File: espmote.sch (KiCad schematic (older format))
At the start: 33 parts, among them J1 Serial, J2 Line, U1 ESP-12E, U2 LM1117-3.3, U3 H11AA1, U4 MOC3023M, U5 H11AA1, U6 MOC3023M, U7 H11AA1, U8 MOC3023M, U9 HLK-PM01

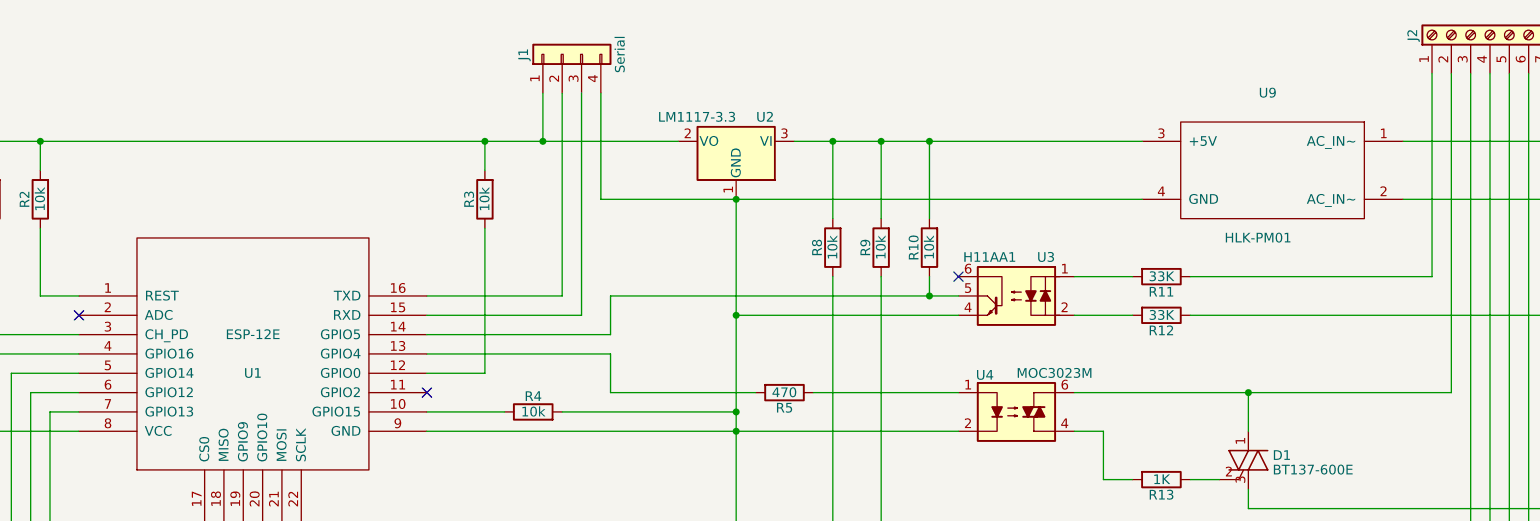
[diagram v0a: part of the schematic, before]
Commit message: Use ESP-12E component from pniaps library
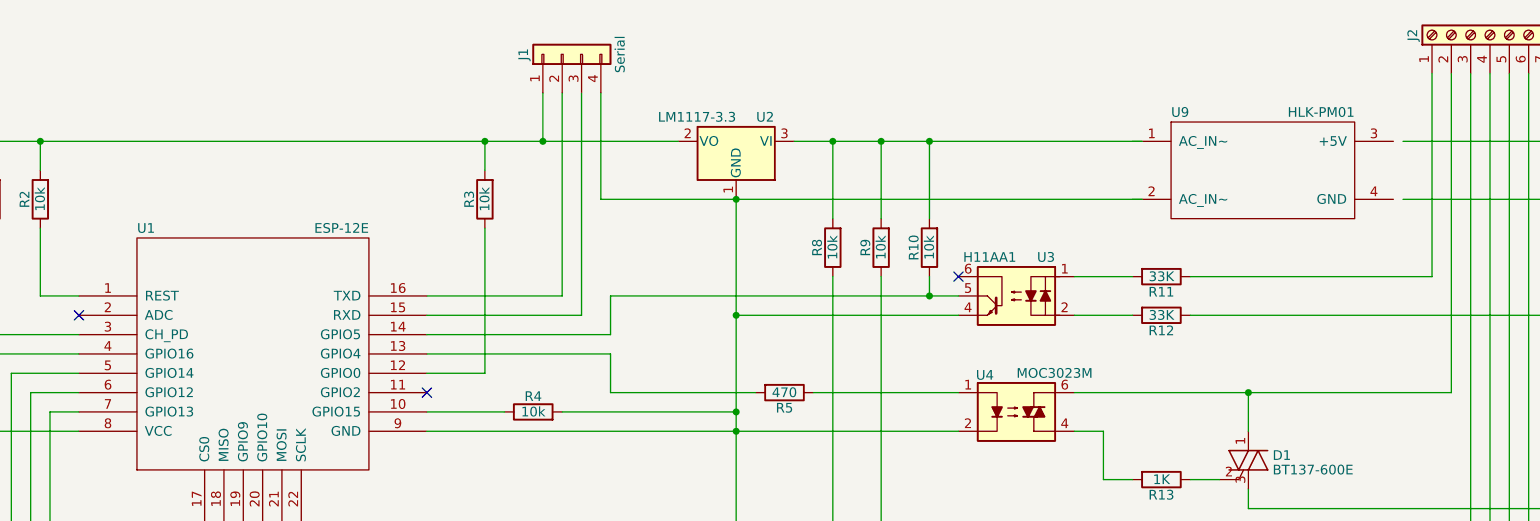
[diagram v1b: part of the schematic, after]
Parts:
- U1: footprint ESP8266:ESP-12E -> pniaps:ESP-12E
- U9: footprint pniaps_lib:HLK-PM01 -> pniaps:HLK-PM01
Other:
- moved on the sheet: U9
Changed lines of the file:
@@
 LIBS:contrib
 LIBS:valves
-LIBS:pnia_kicad
+LIBS:pniaps_kicad
 LIBS:ESP8266
 LIBS:espmote-cache
-EELAYER 25 0
+EELAYER 26 0
 EELAYER END
 $Descr A4 11693 8268
@@
 U 1 1 59A361F9
 P 9000 1500
-F 0 "U9" H 9000 1900 50  0000 C CNN
-F 1 "HLK-PM01" H 9050 1150 50  0000 C CNN
-F 2 "pniaps_lib:HLK-PM01" H 9000 1500 50  0001 C CNN
+F 0 "U9" H 8500 1800 50  0000 L CNN
+F 1 "HLK-PM01" H 9450 1800 50  0000 R CNN
+F 2 "pniaps:HLK-PM01" H 9000 1200 50  0001 C CNN
 F 3 "" H 9000 1500 50  0000 C CNN
 	1    9000 1500
-	-1   0    0    -1
+	1    0    0    -1
 $EndComp
 $Comp
@@
 U 1 1 59A36270
 P 3750 2450
-F 0 "U1" H 3750 2350 50  0000 C CNN
-F 1 "ESP-12E" H 3750 2550 50  0000 C CNN
-F 2 "ESP8266:ESP-12E" H 3750 2450 50  0001 C CNN
+F 0 "U1" H 3150 3100 50  0000 L CNN
+F 1 "ESP-12E" H 4350 3100 50  0000 R CNN
+F 2 "pniaps:ESP-12E" H 3750 2950 50  0001 C CNN
 F 3 "" H 3750 2450 50  0001 C CNN
 	1    3750 2450
@@
 F 0 "U7" H 7500 5250 50  0000 L CNN
 F 1 "H11AA1" H 7700 5250 50  0000 L CNN
-F 2 "Housings_DIP:DIP-6_W7.62mm" H 7500 4850 50  0001 L CIN
+F 2 "Housings_DIP:DIP-6_W7.62mm" H 7700 4850 50  0001 C CIN
 F 3 "" H 7700 5050 50  0001 L CNN
 	1    7700 5050
@@
 F 0 "U5" H 7500 3850 50  0000 L CNN
 F 1 "H11AA1" H 7700 3850 50  0000 L CNN
-F 2 "Housings_DIP:DIP-6_W7.62mm" H 7500 3450 50  0001 L CIN
+F 2 "Housings_DIP:DIP-6_W7.62mm" H 7700 3450 50  0001 C CIN
 F 3 "" H 7700 3650 50  0001 L CNN
 	1    7700 3650
@@
 F 0 "U3" H 7500 2350 50  0000 L CNN
 F 1 "H11AA1" H 7700 2350 50  0000 L CNN
-F 2 "Housings_DIP:DIP-6_W7.62mm" H 7500 1950 50  0001 L CIN
+F 2 "Housings_DIP:DIP-6_W7.62mm" H 7700 1950 50  0001 C CIN
 F 3 "" H 7700 2150 50  0001 L CNN
 	1    7700 2150

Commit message: two channels and pcb
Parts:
- removed D1: BT137-600E, TO_SOT_Packages_THT:TO-220_Vertical, symbol Q_TRIAC_AGA
- removed R10: 10k, Resistors_SMD:R_1206_HandSoldering, symbol R
- removed R11, R12: 33K, Resistors_THT:R_Axial_DIN0414_L11.9mm_D4.5mm_P15.24mm_Horizontal, symbol R
- removed R13: 1K, Resistors_SMD:R_1206_HandSoldering, symbol R
- removed R5: 470, Resistors_SMD:R_1206_HandSoldering, symbol R
- removed U3: H11AA1, Housings_DIP:DIP-6_W7.62mm, symbol H11AA1
- removed U4: MOC3023M, Housings_DIP:DIP-6_W7.62mm, symbol MOC3023M
- J2: footprint Pin_Headers:Pin_Header_Straight_1x08_Pitch2.54mm -> Connectors_Terminal_Blocks:TerminalBlock_Pheonix_MKDS1.5-6pol; symbol Screw_Terminal_01x08 -> Screw_Terminal_01x06
- R14, R15, R17, R18: footprint Resistors_THT:R_Axial_DIN0414_L11.9mm_D4.5mm_P15.24mm_Horizontal -> Resistors_SMD:R_2512_HandSoldering
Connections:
- wire segments 102 -> 78
- no-connect marks 11 -> 12
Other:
- moved on the sheet: U2, U9
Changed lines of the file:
@@
 LIBS:contrib
 LIBS:valves
-LIBS:pniaps_kicad
+LIBS:pniaps
 LIBS:ESP8266
 LIBS:espmote-cache
@@
 F 3 "" H 9000 1500 50  0000 C CNN
 	1    9000 1500
-	1    0    0    -1
+	-1   0    0    -1
 $EndComp
 $Comp
@@
 L LM1117-3.3 U2
 U 1 1 59A3640F
-P 6250 1350
-F 0 "U2" H 6100 1475 50  0000 C CNN
-F 1 "LM1117-3.3" H 6250 1475 50  0000 L CNN
-F 2 "TO_SOT_Packages_THT:TO-220_Vertical" H 6250 1350 50  0001 C CNN
-F 3 "" H 6250 1350 50  0001 C CNN
-	1    6250 1350
+P 7500 1350
+F 0 "U2" H 7350 1475 50  0000 C CNN
+F 1 "LM1117-3.3" H 7500 1475 50  0000 L CNN
+F 2 "TO_SOT_Packages_THT:TO-220_Vertical" H 7500 1350 50  0001 C CNN
+F 3 "" H 7500 1350 50  0001 C CNN
+	1    7500 1350
 	-1   0    0    -1
 $EndComp
@@
 $EndComp
 $Comp
-L Screw_Terminal_01x08 J2
+L Screw_Terminal_01x06 J2
 U 1 1 59A37682
-P 10150 800
-F 0 "J2" H 10150 1200 50  0000 C CNN
-F 1 "Line" H 10150 300 50  0000 C CNN
-F 2 "Pin_Headers:Pin_Header_Straight_1x08_Pitch2.54mm" H 10150 800 50  0001 C CNN
-F 3 "" H 10150 800 50  0001 C CNN
-	1    10150 800
-	0    -1   -1   0
+P 10350 800
+F 0 "J2" H 10350 1200 50  0000 C CNN
+F 1 "Line" H 10350 300 50  0000 C CNN
+F 2 "Connectors_Terminal_Blocks:TerminalBlock_Pheonix_MKDS1.5-6pol" H 10350 800 50  0001 C CNN
+F 3 "" H 10350 800 50  0001 C CNN
+	1    10350 800
+	0    1    -1   0
 $EndComp
 $Comp
@@
 Wire Wire Line
 	8150 4600 8300 4600
-$Comp
-L MOC3023M U4
-U 1 1 59A51C8E
-P 7700 2750
-F 0 "U4" H 7490 2940 50  0000 L CNN
-F 1 "MOC3023M" H 7700 2950 50  0000 L CNN
-F 2 "Housings_DIP:DIP-6_W7.62mm" H 7500 2550 50  0001 L CIN
-F 3 "" H 7675 2750 50  0001 L CNN
-	1    7700 2750
-	1    0    0    -1
-$EndComp
-$Comp
-L H11AA1 U3
-U 1 1 59A51C94
-P 7700 2150
-F 0 "U3" H 7500 2350 50  0000 L CNN
-F 1 "H11AA1" H 7700 2350 50  0000 L CNN
-F 2 "Housings_DIP:DIP-6_W7.62mm" H 7700 1950 50  0001 C CIN
-F 3 "" H 7700 2150 50  0001 L CNN
-	1    7700 2150
-	-1   0    0    -1
-$EndComp
-$Comp
-L Q_TRIAC_AGA D1
-U 1 1 59A51C9A
-P 8900 3000
-F 0 "D1" H 9025 3025 50  0000 L CNN
-F 1 "BT137-600E" H 9025 2950 50  0000 L CNN
-F 2 "TO_SOT_Packages_THT:TO-220_Vertical" V 8975 3025 50  0001 C CNN
-F 3 "" V 8900 3000 50  0001 C CNN
-	1    8900 3000
-	1    0    0    -1
-$EndComp
-$Comp
-L R R13
-U 1 1 59A51CA0
-P 8450 3100
-F 0 "R13" V 8530 3100 50  0000 C CNN
-F 1 "1K" V 8450 3100 50  0000 C CNN
-F 2 "Resistors_SMD:R_1206_HandSoldering" V 8380 3100 50  0001 C CNN
-F 3 "" H 8450 3100 50  0001 C CNN
-	1    8450 3100
-	0    1    1    0
-$EndComp
-$Comp
-L R R5
-U 1 1 59A51CA7
-P 6500 2650
-F 0 "R5" V 6580 2650 50  0000 C CNN
-F 1 "470" V 6500 2650 50  0000 C CNN
-F 2 "Resistors_SMD:R_1206_HandSoldering" V 6430 2650 50  0001 C CNN
-F 3 "" H 6500 2650 50  0001 C CNN
-	1    6500 2650
-	0    1    1    0
-$EndComp
-Wire Wire Line
-	8000 2850 8150 2850
-Wire Wire Line
-	8150 2850 8150 3100
-Wire Wire Line
-	8150 3100 8300 3100
 Wire Wire Line
 	8000 5550 10350 5550
@@
 	10150 4150 10150 1000
 Wire Wire Line
-	8000 2650 9950 2650
-Wire Wire Line
-	9950 2650 9950 1000
-Wire Wire Line
-	8900 3150 8900 3250
-Wire Wire Line
 	8900 4650 8900 4750
-Wire Wire Line
-	8900 2850 8900 2650
-Connection ~ 8900 2650
 Wire Wire Line
 	8900 4350 8900 4150
@@
 	8900 5750 8900 5550
 Connection ~ 8900 5550
-$Comp
-L R R11
-U 1 1 59A52964
-P 8450 2050
-F 0 "R11" V 8530 2050 50  0000 C CNN
-F 1 "33K" V 8450 2050 50  0000 C CNN
-F 2 "Resistors_THT:R_Axial_DIN0414_L11.9mm_D4.5mm_P15.24mm_Horizontal" V 8380 2050 50  0001 C CNN
-F 3 "" H 8450 2050 50  0001 C CNN
-	1    8450 2050
-	0    1    1    0
-$EndComp
-$Comp
-L R R12
-U 1 1 59A52C17
-P 8450 2250
-F 0 "R12" V 8530 2250 50  0000 C CNN
-F 1 "33K" V 8450 2250 50  0000 C CNN
-F 2 "Resistors_THT:R_Axial_DIN0414_L11.9mm_D4.5mm_P15.24mm_Horizontal" V 8380 2250 50  0001 C CNN
-F 3 "" H 8450 2250 50  0001 C CNN
-	1    8450 2250
-	0    1    1    0
-$EndComp
 $Comp
 L R R14
@@
 F 0 "R14" V 8530 3550 50  0000 C CNN
 F 1 "33K" V 8450 3550 50  0000 C CNN
-F 2 "Resistors_THT:R_Axial_DIN0414_L11.9mm_D4.5mm_P15.24mm_Horizontal" V 8380 3550 50  0001 C CNN
+F 2 "Resistors_SMD:R_2512_HandSoldering" V 8380 3550 50  0001 C CNN
 F 3 "" H 8450 3550 50  0001 C CNN
 	1    8450 3550
@@
 F 0 "R15" V 8530 3750 50  0000 C CNN
 F 1 "33K" V 8450 3750 50  0000 C CNN
-F 2 "Resistors_THT:R_Axial_DIN0414_L11.9mm_D4.5mm_P15.24mm_Horizontal" V 8380 3750 50  0001 C CNN
+F 2 "Resistors_SMD:R_2512_HandSoldering" V 8380 3750 50  0001 C CNN
 F 3 "" H 8450 3750 50  0001 C CNN
 	1    8450 3750
@@
 F 0 "R17" V 8530 4950 50  0000 C CNN
 F 1 "33K" V 8450 4950 50  0000 C CNN
-F 2 "Resistors_THT:R_Axial_DIN0414_L11.9mm_D4.5mm_P15.24mm_Horizontal" V 8380 4950 50  0001 C CNN
+F 2 "Resistors_SMD:R_2512_HandSoldering" V 8380 4950 50  0001 C CNN
 F 3 "" H 8450 4950 50  0001 C CNN
 	1    8450 4950
@@
 F 0 "R18" V 8530 5150 50  0000 C CNN
 F 1 "33K" V 8450 5150 50  0000 C CNN
-F 2 "Resistors_THT:R_Axial_DIN0414_L11.9mm_D4.5mm_P15.24mm_Horizontal" V 8380 5150 50  0001 C CNN
+F 2 "Resistors_SMD:R_2512_HandSoldering" V 8380 5150 50  0001 C CNN
 F 3 "" H 8450 5150 50  0001 C CNN
 	1    8450 5150
@@
 $EndComp
 Wire Wire Line
-	8000 2050 8300 2050
-Wire Wire Line
-	8300 2250 8000 2250
-Wire Wire Line
 	8000 3550 8300 3550
 Wire Wire Line
@@
 	8300 5150 8000 5150
 Wire Wire Line
-	6250 2250 7400 2250
-Wire Wire Line
 	6250 5150 7400 5150
 Wire Wire Line
 	6250 3750 7400 3750
 Wire Wire Line
-	2150 1350 5950 1350
+	2150 1350 7200 1350
 Wire Wire Line
 	5250 1100 5250 1350
@@
 	5450 1100 5450 2250
 Wire Wire Line
-	6550 1350 8350 1350
-Wire Wire Line
 	5550 1650 8350 1650
 Wire Wire Line
 	6250 1650 6250 5750
 Connection ~ 6250 3750
-Connection ~ 6250 2250
 Wire Wire Line
 	5550 1100 5550 1650
 Connection ~ 6250 1650
 Wire Wire Line
-	8600 2050 9850 2050
-Wire Wire Line
-	9850 2050 9850 1000
-Wire Wire Line
 	8600 3550 10050 3550
 Wire Wire Line
@@
 Wire Wire Line
 	10550 1000 10550 5150
-Wire Wire Line
-	10550 2250 8600 2250
-Wire Wire Line
-	8900 3250 10450 3250
-Connection ~ 10450 3250
 Wire Wire Line
 	8900 4750 10450 4750
@@
 Wire Wire Line
 	10550 3750 8600 3750
-Connection ~ 10550 2250
 Wire Wire Line
 	10550 5150 8600 5150
@@
 Wire Wire Line
 	2400 2450 2400 5550
-$Comp
-L R R10
-U 1 1 59A61875
-P 7250 1900
-F 0 "R10" V 7330 1900 50  0000 C CNN
-F 1 "10k" V 7250 1900 50  0000 C CNN
-F 2 "Resistors_SMD:R_1206_HandSoldering" V 7180 1900 50  0001 C CNN
-F 3 "" H 7250 1900 50  0001 C CNN
-	1    7250 1900
-	-1   0    0    1
-$EndComp
 $Comp
 L R R9
@@
 $EndComp
 Wire Wire Line
-	7250 1750 7250 1350
-Connection ~ 7250 1350
-Wire Wire Line
-	7000 1750 7000 1350
+	7000 1350 7000 1750
 Connection ~ 7000 1350
 Wire Wire Line
-	6750 1750 6750 1350
+	6750 1350 6750 1750
 Connection ~ 6750 1350
-Wire Wire Line
-	7250 2050 7250 2150
-Connection ~ 7250 2150
 Wire Wire Line
 	7000 2050 7000 3650
@@
 	4650 2750 5050 2750
 Wire Wire Line
-	4650 2850 7400 2850
-Connection ~ 6250 2850
-Wire Wire Line
 	5350 2750 6250 2750
 Connection ~ 6250 2750
 Wire Wire Line
-	5600 2650 6350 2650
-Wire Wire Line
-	6650 2650 7400 2650
-Wire Wire Line
 	4950 2550 4650 2550
-Wire Wire Line
-	5600 2650 5600 2450
-Wire Wire Line
-	5600 2450 4650 2450
-Wire Wire Line
-	5600 2150 7400 2150
-Wire Wire Line
-	5600 2150 5600 2350
-Wire Wire Line
-	5600 2350 4650 2350
 Wire Wire Line
 	5350 2150 4650 2150
@@
 Wire Wire Line
 	2400 5550 6350 5550
-NoConn ~ 7400 2050
 NoConn ~ 7400 3550
 NoConn ~ 7400 4950
 Wire Wire Line
-	8600 3100 8750 3100
-Wire Wire Line
 	8600 4600 8750 4600
 Wire Wire Line
 	8600 6000 8750 6000
+Wire Wire Line
+	4650 2850 6250 2850
+Connection ~ 6250 2850
+NoConn ~ 4650 2450
+NoConn ~ 4650 2350
+Connection ~ 7500 1650
+Wire Wire Line
+	7800 1350 8350 1350
 $EndSCHEMATC

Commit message: Remove detectors
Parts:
- removed R14, R15, R17, R18: 33K, Resistors_SMD:R_2512_HandSoldering, symbol R
- removed R8, R9: 10k, Resistors_SMD:R_1206_HandSoldering, symbol R
- removed U5, U7: H11AA1, Housings_DIP:DIP-6_W7.62mm, symbol H11AA1
- added J3: Switch, Connectors_Terminal_Blocks:TerminalBlock_Pheonix_MKDS1.5-4pol, symbol Screw_Terminal_01x04
- J2: footprint Connectors_Terminal_Blocks:TerminalBlock_Pheonix_MKDS1.5-6pol -> Connectors_Terminal_Blocks:TerminalBlock_Pheonix_MKDS1.5-4pol; symbol Screw_Terminal_01x06 -> Screw_Terminal_01x04
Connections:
- net at J1.4 (Pin_4), R4.2, U1.9 (GND)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: now also J3.2 (Pin_2)
- net at U1.5 (GPIO14): now also J3.4 (Pin_4)
- net at U1.7 (GPIO13): now also J3.3 (Pin_3)
- net at J1.1 (Pin_1), R1.2, R2.2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: now also J3.1 (Pin_1)
- net at J2.4 (Pin_4): now also D2.1 (A1), U6.6
- no-connect marks 12 -> 10
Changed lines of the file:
@@
-$EndComp
-$Comp
-L ESP-12E U1
-U 1 1 59A36270
-P 3750 2450
-F 0 "U1" H 3150 3100 50  0000 L CNN
-F 1 "ESP-12E" H 4350 3100 50  0000 R CNN
-F 2 "pniaps:ESP-12E" H 3750 2950 50  0001 C CNN
-F 3 "" H 3750 2450 50  0001 C CNN
-	1    3750 2450
-	1    0    0    -1
 $EndComp
 $Comp
@@
 $EndComp
 $Comp
-L H11AA1 U7
-U 1 1 59A375C1
-P 7700 5050
-F 0 "U7" H 7500 5250 50  0000 L CNN
-F 1 "H11AA1" H 7700 5250 50  0000 L CNN
-F 2 "Housings_DIP:DIP-6_W7.62mm" H 7700 4850 50  0001 C CIN
-F 3 "" H 7700 5050 50  0001 L CNN
-	1    7700 5050
-	-1   0    0    -1
-$EndComp
-$Comp
-L Screw_Terminal_01x06 J2
+L Screw_Terminal_01x04 J2
 U 1 1 59A37682
-P 10350 800
-F 0 "J2" H 10350 1200 50  0000 C CNN
-F 1 "Line" H 10350 300 50  0000 C CNN
-F 2 "Connectors_Terminal_Blocks:TerminalBlock_Pheonix_MKDS1.5-6pol" H 10350 800 50  0001 C CNN
-F 3 "" H 10350 800 50  0001 C CNN
-	1    10350 800
+P 10450 800
+F 0 "J2" V 10500 1000 50  0000 L CNN
+F 1 "Line" V 10400 1000 50  0000 L CNN
+F 2 "Connectors_Terminal_Blocks:TerminalBlock_Pheonix_MKDS1.5-4pol" H 10450 800 50  0001 C CNN
+F 3 "" H 10450 800 50  0001 C CNN
+	1    10450 800
 	0    1    -1   0
 $EndComp
@@
 U 1 1 59A4F8A3
 P 5350 900
-F 0 "J1" H 5350 1100 50  0000 C CNN
-F 1 "Serial" H 5350 600 50  0000 C CNN
+F 0 "J1" V 5400 600 50  0000 R CNN
+F 1 "Serial" V 5300 600 50  0000 R CNN
 F 2 "Pin_Headers:Pin_Header_Straight_1x04_Pitch2.54mm" H 5350 900 50  0001 C CNN
 F 3 "" H 5350 900 50  0001 C CNN
@@
 NoConn ~ 4650 2650
 Wire Wire Line
-	2150 1350 2150 2850
+	2150 1000 2150 2850
 Wire Wire Line
 	8000 5750 8150 5750
@@
 	1    7700 4250
 	1    0    0    -1
-$EndComp
-$Comp
-L H11AA1 U5
-U 1 1 59A51B09
-P 7700 3650
-F 0 "U5" H 7500 3850 50  0000 L CNN
-F 1 "H11AA1" H 7700 3850 50  0000 L CNN
-F 2 "Housings_DIP:DIP-6_W7.62mm" H 7700 3450 50  0001 C CIN
-F 3 "" H 7700 3650 50  0001 L CNN
-	1    7700 3650
-	-1   0    0    -1
 $EndComp
 $Comp
@@
 	10350 5550 10350 1000
 Wire Wire Line
-	8000 4150 10150 4150
-Wire Wire Line
-	10150 4150 10150 1000
+	8000 4150 10250 4150
 Wire Wire Line
 	8900 4650 8900 4750
@@
 	8900 5750 8900 5550
 Connection ~ 8900 5550
-$Comp
-L R R14
-U 1 1 59A52CE3
-P 8450 3550
-F 0 "R14" V 8530 3550 50  0000 C CNN
-F 1 "33K" V 8450 3550 50  0000 C CNN
-F 2 "Resistors_SMD:R_2512_HandSoldering" V 8380 3550 50  0001 C CNN
-F 3 "" H 8450 3550 50  0001 C CNN
-	1    8450 3550
-	0    1    1    0
-$EndComp
-$Comp
-L R R15
-U 1 1 59A52CE9
-P 8450 3750
-F 0 "R15" V 8530 3750 50  0000 C CNN
-F 1 "33K" V 8450 3750 50  0000 C CNN
-F 2 "Resistors_SMD:R_2512_HandSoldering" V 8380 3750 50  0001 C CNN
-F 3 "" H 8450 3750 50  0001 C CNN
-	1    8450 3750
-	0    1    1    0
-$EndComp
-$Comp
-L R R17
-U 1 1 59A52DC5
-P 8450 4950
-F 0 "R17" V 8530 4950 50  0000 C CNN
-F 1 "33K" V 8450 4950 50  0000 C CNN
-F 2 "Resistors_SMD:R_2512_HandSoldering" V 8380 4950 50  0001 C CNN
-F 3 "" H 8450 4950 50  0001 C CNN
-	1    8450 4950
-	0    1    1    0
-$EndComp
-$Comp
-L R R18
-U 1 1 59A52DCB
-P 8450 5150
-F 0 "R18" V 8530 5150 50  0000 C CNN
-F 1 "33K" V 8450 5150 50  0000 C CNN
-F 2 "Resistors_SMD:R_2512_HandSoldering" V 8380 5150 50  0001 C CNN
-F 3 "" H 8450 5150 50  0001 C CNN
-	1    8450 5150
-	0    1    1    0
-$EndComp
-Wire Wire Line
-	8000 3550 8300 3550
-Wire Wire Line
-	8300 3750 8000 3750
-Wire Wire Line
-	8000 4950 8300 4950
-Wire Wire Line
-	8300 5150 8000 5150
-Wire Wire Line
-	6250 5150 7400 5150
-Wire Wire Line
-	6250 3750 7400 3750
 Wire Wire Line
 	2150 1350 7200 1350
@@
 Wire Wire Line
 	6250 1650 6250 5750
-Connection ~ 6250 3750
 Wire Wire Line
 	5550 1100 5550 1650
 Connection ~ 6250 1650
 Wire Wire Line
-	8600 3550 10050 3550
-Wire Wire Line
-	10050 3550 10050 1000
-Wire Wire Line
-	8600 4950 10250 4950
-Wire Wire Line
-	10250 4950 10250 1000
-Wire Wire Line
 	8900 6050 8900 6150
 Wire Wire Line
@@
 Wire Wire Line
 	10450 6150 10450 1000
-Wire Wire Line
-	10550 1000 10550 5150
 Wire Wire Line
 	8900 4750 10450 4750
 Connection ~ 10450 4750
 Wire Wire Line
-	10550 3750 8600 3750
-Wire Wire Line
-	10550 5150 8600 5150
-Connection ~ 10550 3750
-Wire Wire Line
 	9700 1350 10450 1350
 Connection ~ 10450 1350
 Wire Wire Line
-	9700 1650 10550 1650
-Connection ~ 10550 1650
-Wire Wire Line
-	2700 3650 7400 3650
-Wire Wire Line
-	2700 3650 2700 2750
-Wire Wire Line
 	2600 2650 2600 4150
 Wire Wire Line
-	2500 5050 7400 5050
-Wire Wire Line
-	2500 5050 2500 2550
-Wire Wire Line
 	2400 2450 2400 5550
-$Comp
-L R R9
-U 1 1 59A61B09
-P 7000 1900
-F 0 "R9" V 7080 1900 50  0000 C CNN
-F 1 "10k" V 7000 1900 50  0000 C CNN
-F 2 "Resistors_SMD:R_1206_HandSoldering" V 6930 1900 50  0001 C CNN
-F 3 "" H 7000 1900 50  0001 C CNN
-	1    7000 1900
-	-1   0    0    1
-$EndComp
-$Comp
-L R R8
-U 1 1 59A61B7F
-P 6750 1900
-F 0 "R8" V 6830 1900 50  0000 C CNN
-F 1 "10k" V 6750 1900 50  0000 C CNN
-F 2 "Resistors_SMD:R_1206_HandSoldering" V 6680 1900 50  0001 C CNN
-F 3 "" H 6750 1900 50  0001 C CNN
-	1    6750 1900
-	-1   0    0    1
-$EndComp
-Wire Wire Line
-	7000 1350 7000 1750
-Connection ~ 7000 1350
-Wire Wire Line
-	6750 1350 6750 1750
-Connection ~ 6750 1350
-Wire Wire Line
-	7000 2050 7000 3650
-Connection ~ 7000 3650
-Wire Wire Line
-	6750 2050 6750 5050
-Connection ~ 6750 5050
 Wire Wire Line
 	2150 2850 2850 2850
@@
 	2400 2450 2850 2450
 Wire Wire Line
-	2500 2550 2850 2550
-Wire Wire Line
 	2600 2650 2850 2650
-Wire Wire Line
-	2700 2750 2850 2750
 Wire Wire Line
 	4650 2750 5050 2750
@@
 	5450 2250 4650 2250
 NoConn ~ 2850 2250
-Wire Wire Line
-	7400 4350 6250 4350
 Connection ~ 6250 4350
 Wire Wire Line
 	6250 5750 7400 5750
-Connection ~ 6250 5150
 Wire Wire Line
 	7400 5550 6650 5550
@@
 Wire Wire Line
 	2400 5550 6350 5550
-NoConn ~ 7400 3550
-NoConn ~ 7400 4950
 Wire Wire Line
 	8600 4600 8750 4600
@@
 Wire Wire Line
 	7800 1350 8350 1350
+Wire Wire Line
+	10250 4150 10250 1000
+Wire Wire Line
+	9700 1650 10550 1650
+Wire Wire Line
+	10550 1650 10550 1000
+$Comp
+L Screw_Terminal_01x04 J3
+U 1 1 59FA0F17
+P 2050 800
+F 0 "J3" V 2100 1000 50  0000 L CNN
+F 1 "Switch" V 2000 1000 50  0000 L CNN
+F 2 "Connectors_Terminal_Blocks:TerminalBlock_Pheonix_MKDS1.5-4pol" H 2050 800 50  0001 C CNN
+F 3 "" H 2050 800 50  0001 C CNN
+	1    2050 800
+	0    1    -1   0
+$EndComp
+$Comp
+L ESP-12E U1
+U 1 1 59A36270
+P 3750 2450
+F 0 "U1" H 3150 3100 50  0000 L CNN
+F 1 "ESP-12E" H 4350 3100 50  0000 R CNN
+F 2 "pniaps:ESP-12E" H 3750 2950 50  0001 C CNN
+F 3 "" H 3750 2450 50  0001 C CNN
+	1    3750 2450
+	1    0    0    -1
+$EndComp
+Connection ~ 2150 1350
+Wire Wire Line
+	2050 1000 2050 4350
+Wire Wire Line
+	2050 4350 7400 4350
+Wire Wire Line
+	1950 1000 1950 2750
+Wire Wire Line
+	1950 2750 2850 2750
+Wire Wire Line
+	1850 1000 1850 2550
+Wire Wire Line
+	1850 2550 2850 2550
 $EndSCHEMATC
